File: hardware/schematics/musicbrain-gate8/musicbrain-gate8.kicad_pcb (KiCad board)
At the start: 2 copper layers, 35 x 80 mm, 15 parts, among them J1 BUS, J2 GATES OUT, U1 74HCT595, U2 AMS1117-5.0

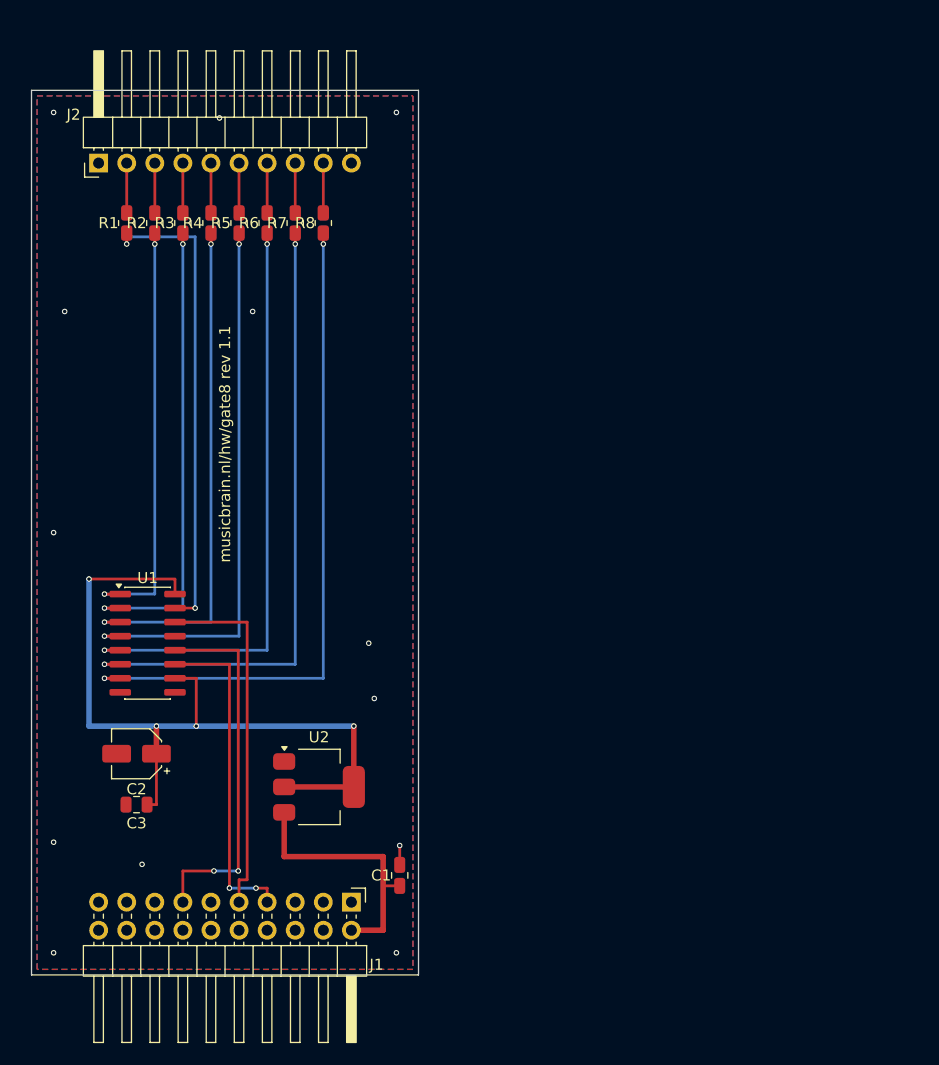
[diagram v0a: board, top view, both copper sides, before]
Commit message: gate8 gen 2: 80x45, slot 2x12, freerouting; generator naar cardlib
- gen_gate.py (schlib+cardlib) vervangt gen_gate_sch.py + gen_gate_pcb_v11.py
  (gen 1, 35x80, eigen sexpr-bouwer van voor cardlib)
- J1 2x10 -> 2x12 via bus.j1_map; J2 1x10 gecentreerd, paneelinzet 4,04
- U1 74HCT595 rot 270: Q-uitgangen noord naar de 1k-kolommen, SPI/GND zuid
- AMS1117-5.0 + ontkoppeling in de oosthelft; +5V blijft lokaal
- prep_dsn.py: DSN-prep (GND-strip + randkrimp) nu een repo-script
- ERC 0, netcheck OK, DRC 0/0

Co-Authored-By: Claude Fable 5 <noreply@anthropic.com>
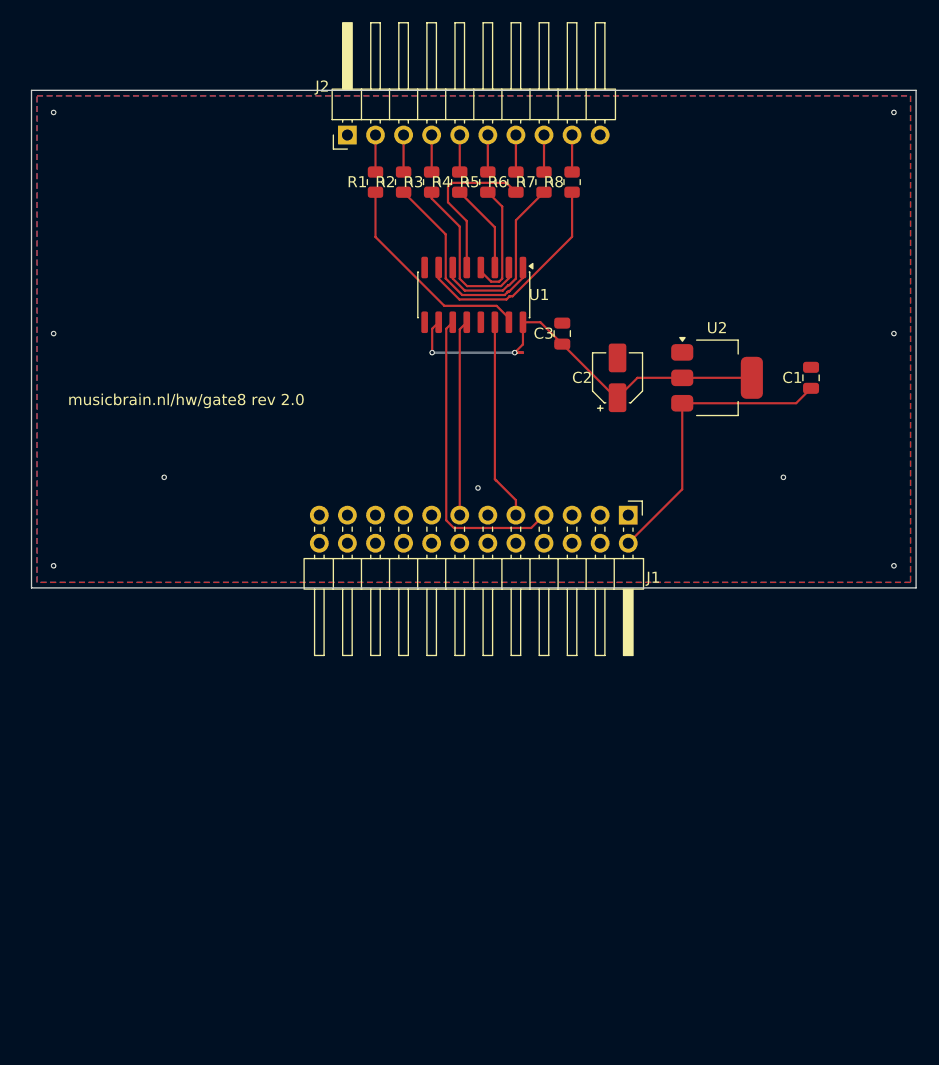
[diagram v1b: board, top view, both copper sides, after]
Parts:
- J1: footprint Connector_PinHeader_2.54mm:PinHeader_2x10_P2.54mm_Horizontal -> Connector_PinHeader_2.54mm:PinHeader_2x12_P2.54mm_Horizontal
- moved C1 58.4 mm to (170.5, 126.0)
- moved C3 57.4 mm to (148.0, 122.0), turned to 90 degrees
- moved C2 55.2 mm to (153.0, 126.0), turned to 90 degrees
- moved U2 51.6 mm to (162.0, 126.0)
- moved U1 43.2 mm to (140.0, 118.5), turned to 270 degrees
- moved J1 43.0 mm to (154.0, 138.4)
- moved R1 22.8 mm to (131.1, 108.3)
- moved R5 22.8 mm to (141.3, 108.3)
- moved R2 22.8 mm to (133.7, 108.3)
- moved R3 22.8 mm to (136.2, 108.3)
- moved R6 22.8 mm to (143.8, 108.3)
- moved R7 22.8 mm to (146.3, 108.3)
- moved R4 22.8 mm to (138.7, 108.3)
- moved R8 22.8 mm to (148.9, 108.3)
- moved J2 22.6 mm to (128.6, 104.0)
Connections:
- net Net-(U1-QA) renamed /QA
- net Net-(U1-QB) renamed /QB
- net Net-(U1-QC) renamed /QC
- net Net-(U1-QD) renamed /QD
- net Net-(U1-QE) renamed /QE
- net Net-(U1-QF) renamed /QF
- net Net-(U1-QG) renamed /QG
- net Net-(U1-QH) renamed /QH
- J1 pad 20: (no net) -> GND
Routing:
- net /QG: track 57.7 -> 16.5 mm, vias 2 -> 0
- net /QH: track 61.5 -> 20.3 mm, vias 2 -> 0
- net /QF: track 53.9 -> 14.7 mm, vias 2 -> 0
- net /QE: track 50.0 -> 11.1 mm, vias 2 -> 0
- net /QD: track 46.2 -> 8.13 mm, vias 2 -> 0
- net +5V: track 72.4 -> 40.8 mm, vias 4 -> 2
- net /QC: track 42.4 -> 14.9 mm, vias 2 -> 0
- net /QA: track 43.2 -> 19.5 mm, vias 2 -> 0
- net /QB: track 38.6 -> 18.6 mm, vias 2 -> 0
- net /CS: track 33.5 -> 17.7 mm, vias 2 -> 0
- net /MOSI: track 32.6 -> 18.5 mm
- net +12V: track 24.0 -> 26.9 mm
- net /SCLK: track 29.8 -> 27.8 mm, vias 2 -> 0
- net GND: track 1.75 -> 0.00 mm, vias 13 -> 9
- net /GATE8: track 4.51 -> 3.35 mm
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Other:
- board size 35 x 80 mm -> 80 x 45 mm
- board text added: "musicbrain.nl/hw/gate8 rev 2.0"
- board text removed: "musicbrain.nl/hw/gate8 rev 1.1"

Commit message: afslank-ronde: potriser 40, gatein8 50, gate8 55, dac8 60, adc8 65 (x45)
80 mm was een maximum, geen eis (observatie Mark): J1/J2 blijven op de
hartlijn, de rand schuift naar binnen. Silk verticaal in de westrand
(horizontaal paste niet meer); hoekvia's geparametriseerd op BX0/BX1;
zwervers mee (gate8 C1, dac8 C3, adc8 JP1). Alle vijf opnieuw geroute
(verse SES) en op ERC 0 + netcheck OK + DRC 0/0.

Co-Authored-By: Claude Fable 5 <noreply@anthropic.com>
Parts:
- moved C1 11.0 mm to (162.0, 119.0)
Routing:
- net /QB: track 18.6 -> 32.2 mm
- net /QA: track 19.5 -> 25.0 mm
- net +5V: track 40.8 -> 45.0 mm, vias 2 -> 0
- net /QE: track 11.1 -> 7.08 mm
- net /QD: track 8.13 -> 11.6 mm
- net +12V: track 26.9 -> 24.3 mm
- net /QF: track 14.7 -> 12.4 mm
- net /QH: track 20.3 -> 19.7 mm
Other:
- board size 80 x 45 mm -> 55 x 45 mm
